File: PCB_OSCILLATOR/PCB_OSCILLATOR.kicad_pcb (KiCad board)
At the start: 2 copper layers, 70 parts, among them P1 POWER SUPPLY, P2 SPI_AD5270_1, P3 SPI_AD5270_2, P4 SPI_AD9833_1, P5 SPI_AD9833_2, U1 AD5270, U2 AD8421, U3 AD9833, U4 AD5270, U5 AD8421, U6 AD9833, U7 ADG819

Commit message: Primera Versión completa con diagrama de bloques en carpeta principal
//
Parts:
- removed R1, R10, R11, R2, R3, R4, R5, R6, R7, R8, R9: 0R, Resistors_SMD:R_0805_HandSoldering
- removed W1: TEST_8, Measurement_Points:Measurement_Point_Round-TH_Small
- removed W3: TEST_9, Measurement_Points:Measurement_Point_Round-TH_Small
- removed W5: TEST_10, Measurement_Points:Measurement_Point_Round-TH_Small
- removed W7: TEST_11, Measurement_Points:Measurement_Point_Round-TH_Small
- removed W9: TEST_12, Measurement_Points:Measurement_Point_Round-TH_Small
- added C28: 0.1uF, Resistors_SMD:R_0805_HandSoldering, F.Cu at (248.0, 62.2)
- added C29: 10uF, Resistors_SMD:R_0805_HandSoldering, F.Cu at (253.3, 62.2)
- added J1: Jumper, Pin_Headers:Pin_Header_Straight_1x02, F.Cu at (252.9, 84.3)
- added J10: Jumper, Pin_Headers:Pin_Header_Straight_1x02, F.Cu at (264.8, 84.3)
- added J11: Jumper, Pin_Headers:Pin_Header_Straight_1x02, F.Cu at (270.9, 84.6)
- added J2: Jumper, Pin_Headers:Pin_Header_Straight_1x02, F.Cu at (258.9, 84.3)
- added J3: Jumper, Pin_Headers:Pin_Header_Straight_1x02, F.Cu at (248.9, 94.4)
- added J4: Jumper, Pin_Headers:Pin_Header_Straight_1x02, F.Cu at (239.3, 87.6)
- added J5: Jumper, Pin_Headers:Pin_Header_Straight_1x02, F.Cu at (254.9, 94.4)
- added J6: Jumper, Pin_Headers:Pin_Header_Straight_1x02, F.Cu at (247.0, 84.3)
- added J7: Jumper, Pin_Headers:Pin_Header_Straight_1x02, F.Cu at (260.8, 94.4)
- added J8: Jumper, Pin_Headers:Pin_Header_Straight_1x02, F.Cu at (242.6, 94.7)
- added J9: Jumper, Pin_Headers:Pin_Header_Straight_1x02, F.Cu at (266.0, 94.2)
- moved W14 115.5 mm to (274.8, 63.1)
- moved W6 91.4 mm to (264.3, 70.3)
- moved R12 88.9 mm to (248.0, 68.5)
- moved C12 86.1 mm to (252.8, 74.8)
- moved C15 85.4 mm to (267.3, 57.8)
- moved C13 85.4 mm to (258.5, 63.2)
- moved C16 83.8 mm to (247.6, 74.8)
- moved C17 83.8 mm to (253.2, 68.5)
- moved D1 73.2 mm to (273.3, 127.4)
- moved W2 71.8 mm to (258.3, 75.7)
- moved C8 71.6 mm to (269.3, 64.1)
- moved W10 68.2 mm to (275.6, 69.2)
- moved C6 68.1 mm to (274.4, 142.3)
- moved C11 67.3 mm to (258.7, 69.5)
- moved C20 62.6 mm to (278.0, 103.6)
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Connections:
- P2 pad 5: /VDD -> (no net)
- P2 pad 6: /GND -> (no net)
- P3 pad 5: /VDD -> (no net)
- P3 pad 6: /GND -> (no net)
- P4 pad 5: /VDD -> (no net)
- P4 pad 6: /GND -> (no net)
- P5 pad 4: /VDD -> (no net)
- P5 pad 5: /VDD -> (no net)
- P5 pad 6: /GND -> (no net)

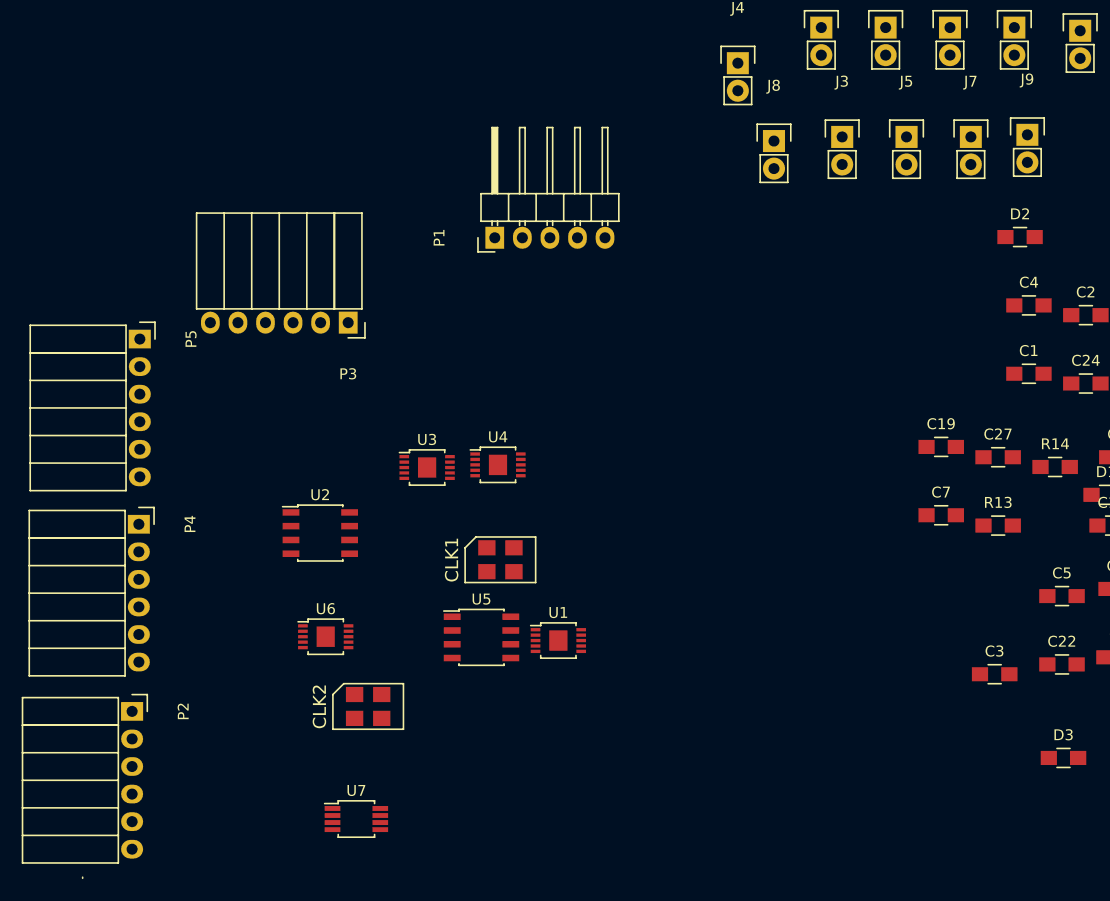
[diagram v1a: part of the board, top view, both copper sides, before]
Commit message: SEGREGANDO ELEMENTOS SIN VER CAMINOS NI CAPACITORES
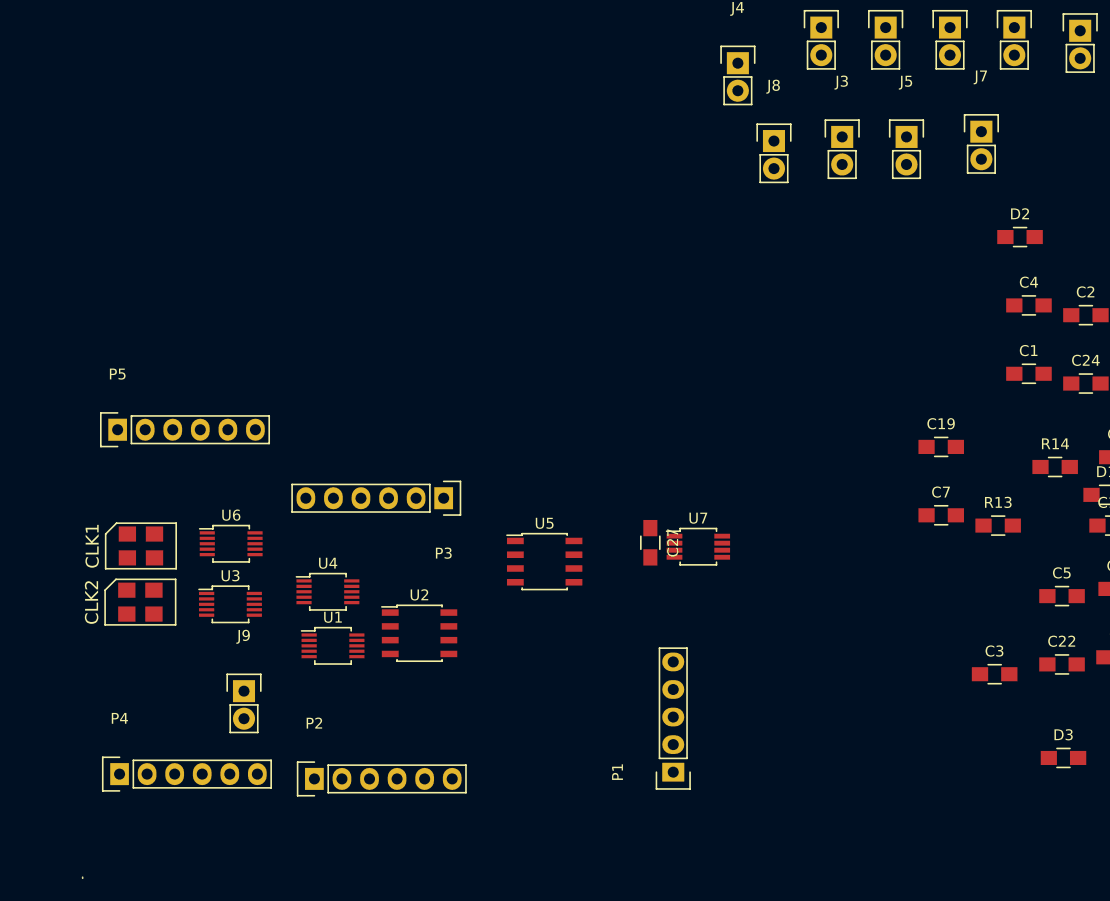
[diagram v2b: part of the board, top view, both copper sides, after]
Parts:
- P1: footprint Pin_Headers:Pin_Header_Angled_1x05 -> Socket_Strips:Socket_Strip_Straight_1x05
- P2, P3, P4, P5: footprint Socket_Strips:Socket_Strip_Angled_1x06 -> Socket_Strips:Socket_Strip_Straight_1x06
- U1, U3, U4, U6: footprint Housings_SSOP:MSOP-10-1EP_3x3mm_Pitch0.5mm -> Housings_SSOP:MSOP-10_3x3mm_Pitch0.5mm
- moved J9 88.6 mm to (193.8, 145.4)
- moved P1 51.9 mm to (233.4, 152.9)
- moved U7 40.3 mm to (235.7, 132.1)
- moved CLK1 33.2 mm to (184.3, 132.1)
- moved C27 33.0 mm to (231.3, 131.8), turned to 270 degrees
- moved P4 23.1 mm to (182.3, 153.1), turned to 0 degrees
- moved CLK2 23.1 mm to (184.3, 137.2)
- moved U3 22.1 mm to (192.6, 137.4)
- moved U1 20.8 mm to (202.0, 141.3)
- moved U4 19.6 mm to (201.5, 136.3)
- moved P3 18.4 mm to (212.2, 127.7)
- moved P2 17.9 mm to (200.3, 153.5), turned to 0 degrees
- moved U2 13.0 mm to (210.0, 140.1)
- moved U6 12.2 mm to (192.6, 131.9)
- moved U5 9.09 mm to (221.5, 133.5)
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
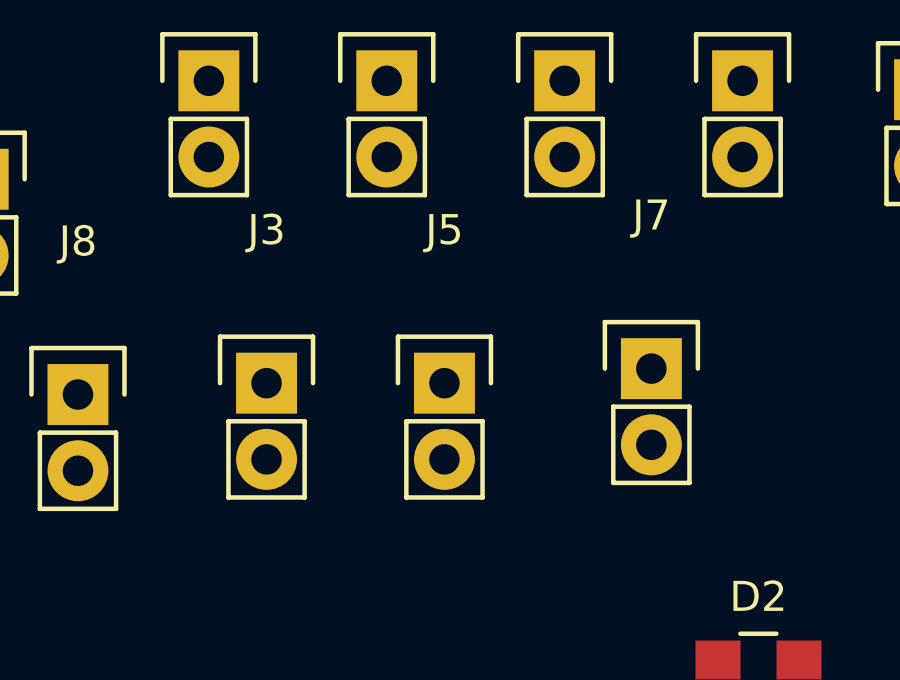
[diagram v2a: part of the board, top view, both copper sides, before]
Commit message: Faltan Hacer correciones que están en trello
Terminar correciones y pasar a la etapa de segregación de elementos,
layout final propuesto para el viernes 12
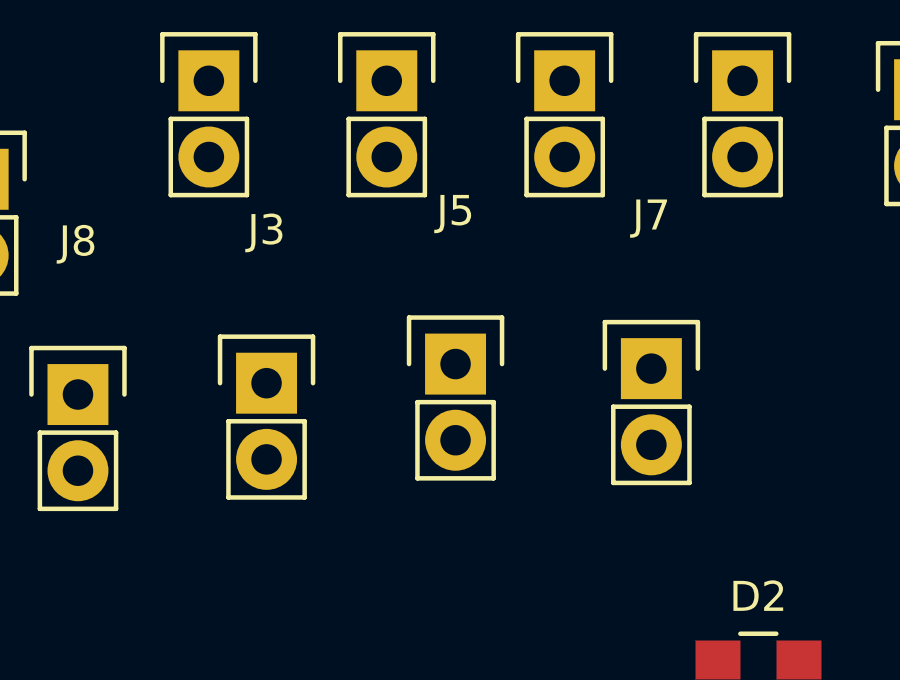
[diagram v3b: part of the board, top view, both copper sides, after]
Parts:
- moved J5 0.74 mm to (255.2, 93.7)
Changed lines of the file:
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@@
   )
   (module Pin_Headers:Pin_Header_Straight_1x02 (layer F.Cu)
-    (at 254.861796 94.36372)
+    (at 255.2319 93.726)
     (descr "Through hole pin header")
     (tags "pin header")

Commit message: Algunos cambios Adicionales
//
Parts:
- added C30: 1uF, Capacitors_SMD:C_0805_HandSoldering, F.Cu at (249.5, 97.4)
- added C31: 0.47uF, Capacitors_SMD:C_1206_HandSoldering, F.Cu at (220.0, 92.3)
- added C32: 0.1uF, Resistors_SMD:R_0805_HandSoldering, F.Cu at (234.9, 98.6)
- added C33: 0.1uF, Resistors_SMD:R_0805_HandSoldering, F.Cu at (229.5, 104.9)
- added C34: 10uF, Resistors_SMD:R_0805_HandSoldering, F.Cu at (249.5, 85.0)
- added C35: 0.1uF, Resistors_SMD:R_0805_HandSoldering, F.Cu at (209.9, 126.4)
- added C36: 10uF, Resistors_SMD:R_0805_HandSoldering, F.Cu at (243.1, 91.3)
- added C37: 0.1uF, Resistors_SMD:R_0805_HandSoldering, F.Cu at (221.5, 117.3)
- added C38: 10uF, Resistors_SMD:R_0805_HandSoldering, F.Cu at (247.5, 91.3)
- added C39: 0.1uF, Resistors_SMD:R_0805_HandSoldering, F.Cu at (216.8, 117.3)
- added J12: Jumper, Pin_Headers:Pin_Header_Straight_1x02, F.Cu at (184.8, 100.5)
- added J13: Jumper, Pin_Headers:Pin_Header_Straight_1x02, F.Cu at (207.4, 81.7)
- added J14: Jumper, Pin_Headers:Pin_Header_Straight_1x02, F.Cu at (228.9, 139.3)
- added J15: Jumper, Pin_Headers:Pin_Header_Straight_1x02, F.Cu at (223.0, 150.0)
- added J16: Jumper, Pin_Headers:Pin_Header_Straight_1x02, F.Cu at (217.0, 148.3)
- added R1: 1K, Resistors_SMD:R_0805_HandSoldering, F.Cu at (233.1, 111.0)
- added R2: 100K, Resistors_SMD:R_0805_HandSoldering, F.Cu at (227.5, 117.1)
- added R3: 1K, Resistors_SMD:R_0805_HandSoldering, F.Cu at (245.1, 97.4)
- added R4: 10K, Resistors_SMD:R_0805_HandSoldering, F.Cu at (239.7, 110.8)
- added U10: ADR291, TO_SOT_Packages_THT:TO-92_Inline_Narrow_Oval, F.Cu at (161.2, 90.6)
- added U8: ADP3303, Housings_SOIC:SOIC-8_3.9x4.9mm_Pitch1.27mm, F.Cu at (179.3, 62.0)
- added U9: AD8651, Housings_SOIC:SOIC-8_3.9x4.9mm_Pitch1.27mm, F.Cu at (155.6, 97.4)
- added W1: TEST_8, Measurement_Points:Measurement_Point_Round-TH_Small, F.Cu at (232.5, 117.1)
- added W11: TEST_13, Measurement_Points:Measurement_Point_Round-TH_Small, F.Cu at (230.5, 155.7)
- added W13: TEST_14, Measurement_Points:Measurement_Point_Round-TH_Small, F.Cu at (206.9, 95.3)
- added W3: TEST_9, Measurement_Points:Measurement_Point_Round-TH_Small, F.Cu at (227.6, 123.2)
- added W5: TEST_10, Measurement_Points:Measurement_Point_Round-TH_Small, F.Cu at (200.6, 109.3)
- added W7: TEST_11, Measurement_Points:Measurement_Point_Round-TH_Small, F.Cu at (213.5, 95.3)
- added W9: TEST_12, Measurement_Points:Measurement_Point_Round-TH_Small, F.Cu at (206.9, 101.4)
- C1, C13, C19, C7: footprint Resistors_SMD:R_0805_HandSoldering -> Capacitors_SMD:C_1206_HandSoldering
- moved P1 115.9 mm to (172.4, 54.4), turned to 180 degrees
- moved C10 92.0 mm to (193.3, 122.8)
- moved P4 87.3 mm to (134.9, 79.8)
- moved D3 86.7 mm to (222.2, 78.8)
- moved U5 81.2 mm to (143.0, 112.8)
- moved C26 80.9 mm to (199.2, 128.1)
- moved P2 78.5 mm to (125.3, 130.4)
- moved P3 77.5 mm to (137.6, 106.9)
- moved W10 76.3 mm to (221.9, 123.4)
- moved J10 75.7 mm to (211.1, 137.7)
- moved J11 75.3 mm to (195.6, 81.8)
- moved U7 74.7 mm to (167.5, 101.6)
- moved C2 72.5 mm to (199.7, 121.8)
- moved C1 72.3 mm to (193.9, 116.6)
- moved C28 72.1 mm to (205.2, 120.2)
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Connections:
- net /+18V renamed /+12V
- net /-18V renamed /-12V
- net /WAVE_AD8421_1 renamed /BASE_WAVE
- net /WAVE_AD8421_2 renamed /FINAL_WAVE
- C28 pad 1: /VDD -> /+5V
- C29 pad 1: /VDD -> /+5V
- CLK1 pad 1: /VDD -> Net-(CLK1-Pad1)
- CLK2 pad 1: /VDD -> Net-(CLK2-Pad1)
- D2 pad 2: /VDD -> /+5V
- P1 pad 1: /VDD -> /+5V
- U2 pad 6: /GND -> Net-(J12-Pad1)
- U5 pad 6: /GND -> Net-(J13-Pad1)
- U7 pad 6: /WAVE_DDS_2 -> /MODULATING_WAVE
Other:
- board outline added: 161.6 x 129 mm
